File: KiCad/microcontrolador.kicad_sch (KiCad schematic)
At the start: 0 parts

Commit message: he canviat el micro
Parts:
- added C2: 10uF, symbol Device:C
- added C21, C5: 100nF, symbol Device:C
- added C6, C7, C8: 0.1uF, symbol Device:C
- added PIC32MX254F128B1: ~, projecte_llums:PIC32MX254F128B, symbol PROJECTE_LLUMS:PIC32MX254F128B
- added R1, R18: 10K, symbol Device:R
- added U7: PIC24HJ128GP502-I_SO, PIC24HJ128GP502-I_SO:SOIC127P1030X265-28N, symbol PIC24HJ128GP502-I_SO:PIC24HJ128GP502-I_SO
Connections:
- new net: C21.1, PIC32MX254F128B1.1 (MCLR), R18.2
- new net: C2.2, PIC32MX254F128B1.20 (VCAP)
- new net: C5.1, R1.1, U7.1 (~{MCLR})
- new net: C8.1, U7.20 (VCAP)
- new net 3V3: PIC32MX254F128B1.28 (AVDD), R1.2, R18.1
- new net 5V: C6.1, C7.1, PIC32MX254F128B1.13 (VDD), U7.13 (VDD), U7.28 (AVDD)
- new net CANRX: PIC32MX254F128B1.17 (CANRX), U7.15 (PGEC3/ASCL1/RP6/CN24/PMD6/RB6)
- new net CANTX: PIC32MX254F128B1.18 (CANTX), U7.11 (SOSCI/RP4/CN1/PMBE/RB4)
- new net CARRETERA: PIC32MX254F128B1.12 (RA4), U7.21 (PGED2/TDI/RP10/CN16/PMD2/RB10)
- new net DIURNA: PIC32MX254F128B1.21 (RB10), U7.23 (AN12/RP12/CN14/PMD0/RB12)
- new net ENCREUAMENT: PIC32MX254F128B1.14 (RB5), U7.22 (PGEC2/TMS/RP11/CN15/PMD1/RB11)
- new net GND: C2.1, C21.2, C5.2, C6.2, C7.2, C8.2, PIC32MX254F128B1.19 (VSS), PIC32MX254F128B1.27 (AVSS), PIC32MX254F128B1.8 (VSS), U7.19 (VSS), U7.27 (AVSS), U7.8 (VSS)
- new net I2C_SCL: PIC32MX254F128B1.5 (I2C_SCL), U7.17 (TCK/SCL1/RP8/CN22/PMD4/RB8)
- new net I2C_SDA: PIC32MX254F128B1.6 (I2C_SDA), U7.18 (TDO/SDA1/RP9/CN21/PMD3/RB9)
- new net INTERM. DRT: PIC32MX254F128B1.23 (RB12), U7.25 (AN10/RTCC/RP14/CN12/PMWR/RB14)
- new net INTERM. ESQ: PIC32MX254F128B1.22 (RB11), U7.24 (AN11/RP13/CN13/PMRD/RB13)
- new net NETEJA-FARS: PIC32MX254F128B1.24 (RB13), U7.26 (AN9/RP15/CN11/PMCS1/RB15)
- new net PMW: PIC32MX254F128B1.25 (PWM), U7.6 (AN4/C1IN-/RP2/CN6/RB2)
- new net UART_RX: PIC32MX254F128B1.16 (UART_RX), U7.16 (INT0/RP7/CN23/PMD5/RB7)
- new net UART_TX: PIC32MX254F128B1.15 (UART_TX), U7.14 (PGED3/ASDA1/RP5/CN27/PMD7/RB5)
- no-connect marks 0 -> 16
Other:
- note added: "MICROCONTROLADOR"
- note added: "Pull up a prop del pin MCLR"

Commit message: ERC i footprints
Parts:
- C5, C6, C7, C8: footprint (none) -> Capacitor_SMD:C_0805_2012Metric_Pad1.18x1.45mm_HandSolder
- R1: footprint (none) -> Resistor_SMD:R_0805_2012Metric_Pad1.20x1.40mm_HandSolder
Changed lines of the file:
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@@
+		(color 0 0 0 0)
+	)
+	(junction
+		(at 194.31 67.31)
+		(diameter 0)
 		(color 0 0 0 0)
 	)
@@
 	)
 	(symbol
+		(lib_id "power:PWR_FLAG")
+		(at 194.31 67.31 180)
+		(unit 1)
+		(exclude_from_sim no)
+		(in_bom yes)
+		(on_board yes)
+		(dnp no)
+		(property "Reference" "#FLG05"
+			(at 194.31 69.215 0)
+			(effects
+				(font
+					(size 1.27 1.27)
+				)
+				(hide yes)
+			)
+		)
+		(property "Value" "PWR_FLAG"
+			(at 194.818 71.374 0)
+			(effects
+				(font
+					(size 1.27 1.27)
+				)
+			)
+		)
+		(property "Footprint" ""
+			(at 194.31 67.31 0)
+			(effects
+				(font
+					(size 1.27 1.27)
+				)
+				(hide yes)
+			)
+		)
+		(property "Datasheet" "~"
+			(at 194.31 67.31 0)
+			(effects
+				(font
+					(size 1.27 1.27)
+				)
+				(hide yes)
+			)
+		)
+		(property "Description" "Special symbol for telling ERC where power comes from"
+			(at 194.31 67.31 0)
+			(effects
+				(font
+					(size 1.27 1.27)
+				)
+				(hide yes)
+			)
+		)
+		(pin "1"
+		)
+		(instances
+			(project ""
+				(path "/b4874c87-978f-427f-bc45-3635f8629977/65403977-6a27-47ce-ace7-4876548c1d8f"
+					(reference "#FLG05")
+					(unit 1)
+				)
+			)
+		)
+	)
+	(symbol
 		(lib_id "PROJECTE_LLUMS:PIC32MX254F128B")
 		(at -55.88 92.71 0)
@@
 			)
 		)
-		(property "Footprint" ""
+		(property "Footprint" "Resistor_SMD:R_0805_2012Metric_Pad1.20x1.40mm_HandSolder"
 			(at 80.518 64.77 90)
 			(effects
@@
 			)
 		)
-		(property "Footprint" ""
+		(property "Footprint" "Capacitor_SMD:C_0805_2012Metric_Pad1.18x1.45mm_HandSolder"
 			(at 227.0252 72.39 0)
 			(effects
@@
 			)
 		)
-		(property "Footprint" ""
+		(property "Footprint" "Capacitor_SMD:C_0805_2012Metric_Pad1.18x1.45mm_HandSolder"
 			(at 79.7052 82.55 0)
 			(effects
@@
 			)
 		)
-		(property "Footprint" ""
+		(property "Footprint" "Capacitor_SMD:C_0805_2012Metric_Pad1.18x1.45mm_HandSolder"
 			(at 237.1852 69.85 0)
 			(effects
@@
 			)
 		)
-		(property "Footprint" ""
+		(property "Footprint" "Capacitor_SMD:C_0805_2012Metric_Pad1.18x1.45mm_HandSolder"
 			(at 216.8652 74.93 0)
 			(effects

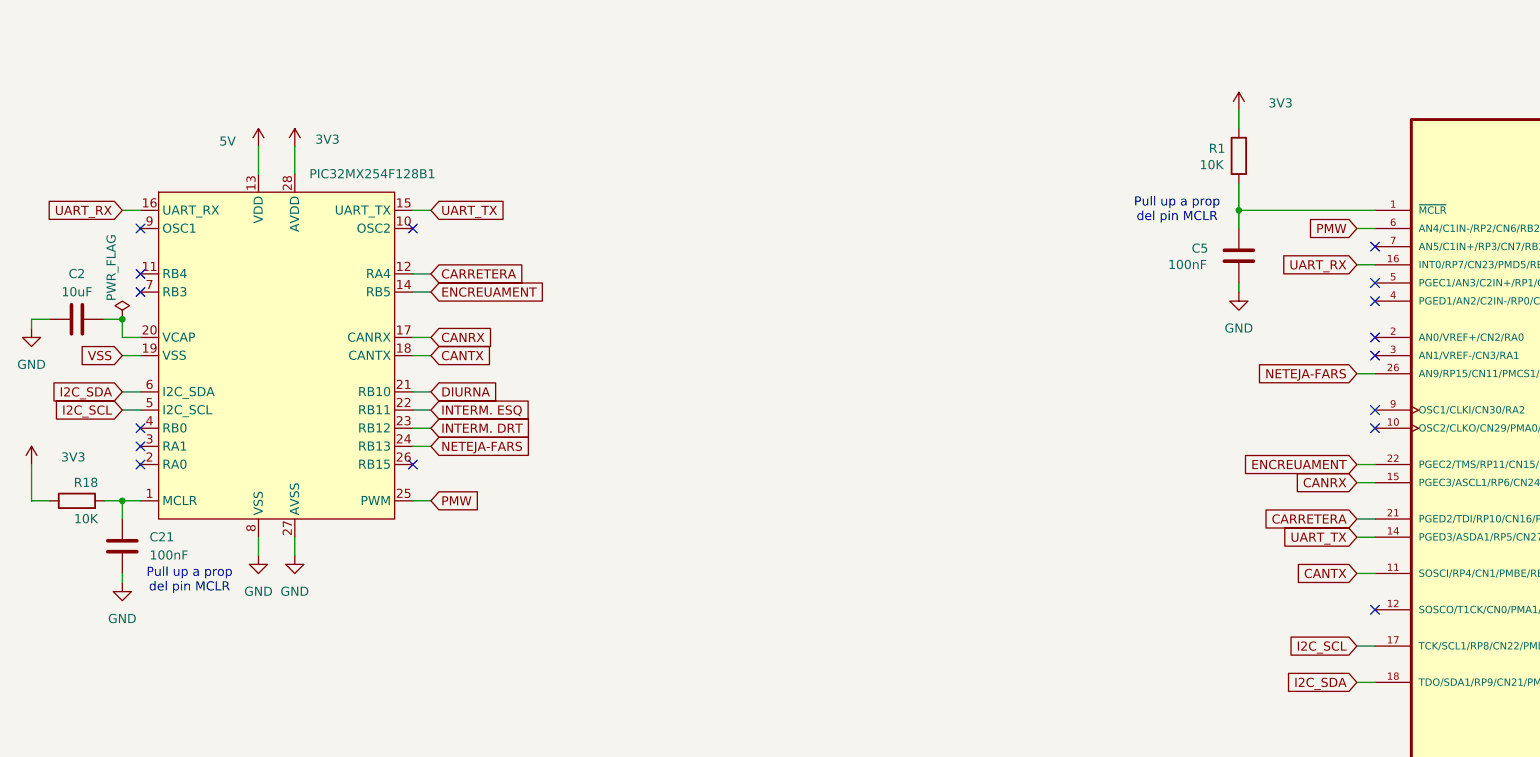
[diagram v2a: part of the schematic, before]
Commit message: placement (falten LEDs)
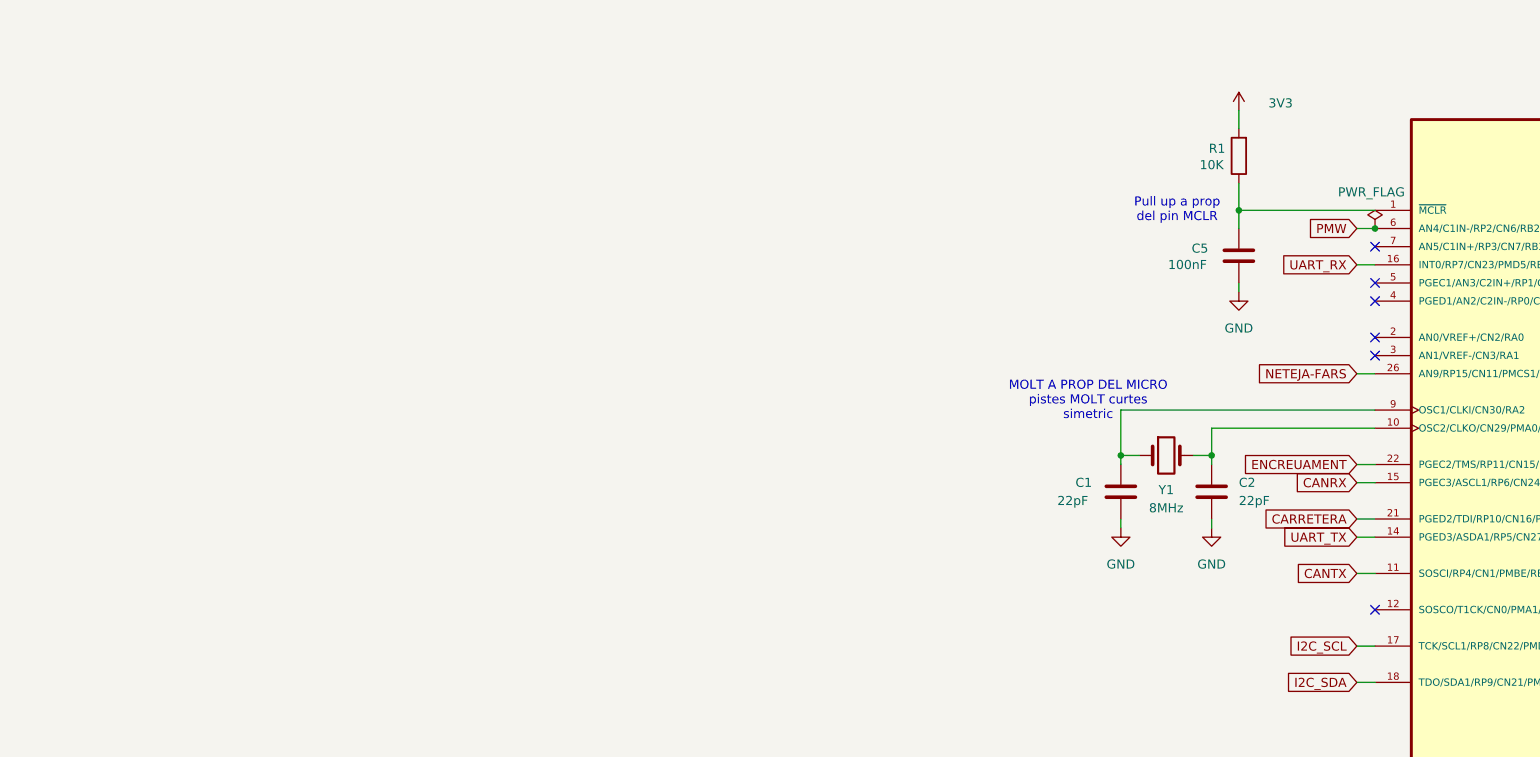
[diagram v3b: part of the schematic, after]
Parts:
- removed C21: 100nF, symbol Device:C
- removed PIC32MX254F128B1: ~, projecte_llums:PIC32MX254F128B, symbol PROJECTE_LLUMS:PIC32MX254F128B
- removed R18: 10K, symbol Device:R
- added C1: 22pF, Capacitor_SMD:C_0805_2012Metric_Pad1.18x1.45mm_HandSolder, symbol Device:C
- added Y1: 8MHz, Crystal:Crystal_SMD_3225-4Pin_3.2x2.5mm_HandSoldering, symbol Device:Crystal
- C2: value 10uF -> 22pF; footprint (none) -> Capacitor_SMD:C_0805_2012Metric_Pad1.18x1.45mm_HandSolder
- U7: footprint PIC24HJ128GP502-I_SO:SOIC127P1030X265-28N -> footprints:SOIC127P1030X265-28N
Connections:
- net GND: now also C2.2, C1.2; no longer C2.1
- net at U7.10 (OSC2/CLKO/CN29/PMA0/RA3): now also C2.1, Y1.2
- net at U7.9 (OSC1/CLKI/CN30/RA2): now also C1.1, Y1.1
- no-connect marks 16 -> 6
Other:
- note added: "MOLT A PROP DEL MICRO pistes MOLT curtes simetric"

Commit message: routing
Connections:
- net /MCLR: now reaches C5.1, R1.1, U7.1 (~{MCLR})
- net OSC2: now reaches C2.1, U7.10 (OSC2/CLKO/CN29/PMA0/RA3), Y1.2
- net VCAP: now reaches C8.1, U7.20 (VCAP)
- net OSC1: now reaches C1.1, U7.9 (OSC1/CLKI/CN30/RA2), Y1.1
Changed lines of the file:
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@@
+		)
+	)
+	(label "{slash}MCLR"
+		(at 83.82 72.39 0)
+		(effects
+			(font
+				(size 1.27 1.27)
+			)
+			(justify left bottom)
+		)
+	)
+	(label "VCAP"
+		(at 200.66 67.31 0)
+		(effects
+			(font
+				(size 1.27 1.27)
+			)
+			(justify left bottom)
+		)
+	)
+	(label "OSC1"
+		(at 81.28 100.33 0)
+		(effects
+			(font
+				(size 1.27 1.27)
+			)
+			(justify left bottom)
+		)
+	)
+	(label "OSC2"
+		(at 81.28 102.87 0)
+		(effects
+			(font
+				(size 1.27 1.27)
+			)
+			(justify left bottom)
 		)
 	)

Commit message: correcció d'errors CADLAB, falten els de llums i un parell que no entenc
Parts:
- added J3: Conn_01x03, Connector_PinHeader_2.54mm:PinHeader_1x03_P2.54mm_Vertical, symbol Connector_Generic:Conn_01x03
- added R16, R17: 100, Resistor_SMD:R_0805_2012Metric_Pad1.20x1.40mm_HandSolder, symbol Device:R
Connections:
- net GND: now also J3.3 (Pin_3)
- net UART_RX: now also R17.1
- net UART_TX: now also R16.1
- new net CON1: J3.1 (Pin_1), R16.2
- new net CON2: J3.2 (Pin_2), R17.2
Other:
- note added: "USART/DEBUG"
- moved on the sheet: C1, C2, C5, C6, C7, C8, R1, U7, Y1

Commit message: alguns errors de CADLAB i he canivat d'ordre els LEDs i els drivers a la PCB.
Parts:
- removed J3: Conn_01x03, Connector_PinHeader_2.54mm:PinHeader_1x03_P2.54mm_Vertical, symbol Connector_Generic:Conn_01x03
- removed R16, R17: 100, Resistor_SMD:R_0805_2012Metric_Pad1.20x1.40mm_HandSolder, symbol Device:R
- added J2: DE9_Pins_MountingHoles, Connector_Dsub:DSUB-9_Pins_Horizontal_P2.77x2.84mm_EdgePinOffset4.94mm_Housed_MountingHolesOffset4.94mm, symbol Connector:DE9_Pins_MountingHoles
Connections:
- net GND: now also J2.5
- net UART_RX: now also J2.2
- net UART_TX: now also J2.3
- net 3V3 renamed +3V3
- net 5V renamed +5V
- net +5V: now also J2.1
- no-connect marks 6 -> 12
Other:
- note added: "2026-04-20"
- note added: "Curs 2025/2026 Eines de Disseny Martina Camprubí, Clara Rosaura Universitat de Barcelona"
- note added: "Placa Pràctica 5"

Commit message: modificacions cadlab
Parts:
- removed U7: PIC24HJ128GP502-I_SO, footprints:SOIC127P1030X265-28N, symbol PIC24HJ128GP502-I_SO:PIC24HJ128GP502-I_SO
- added C_out3: 100nF, Capacitor_SMD:C_0805_2012Metric_Pad1.18x1.45mm_HandSolder, symbol Device:C
- added J5: DE9_Pins_MountingHoles, Connector_Dsub:DSUB-9_Pins_Horizontal_P2.77x2.84mm_EdgePinOffset4.94mm_Housed_MountingHolesOffset4.94mm, symbol Connector:DE9_Pins_MountingHoles
- added R13: 12O, Resistor_SMD:R_0805_2012Metric_Pad1.20x1.40mm_HandSolder, symbol Device:R
- added R14: 10k, Resistor_SMD:R_0805_2012Metric_Pad1.20x1.40mm_HandSolder, symbol Device:R
- added U2: ~, symbol PROJECTE_LLUMS:PIC24HJ128GP502
- added U4: MCP2551-I-SN, Package_SO:SOIC-8_3.9x4.9mm_P1.27mm, symbol Interface_CAN_LIN:MCP2551-I-SN
- added U7: PIC24HJ128GP502, projecte_llums:SOIC127P1030X265-28N, symbol PROJECTE_LLUMS:PIC24HJ128GP502
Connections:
- net +5V: now also J5.1, U7.13 (VDD), U7.28 (AVDD)
- net CANRX: now also U4.4 (RXD), U7.15 (CANRX)
- net CANTX: now also U4.1 (TXD), U7.11 (CANTX)
- net CARRETERA: now also U7.21 (RB10)
- net DIURNA: now also U7.23 (RB12)
- net ENCREUAMENT: now also U7.22 (RB11)
- net GND: now also C_out3.1, J5.5, R14.2, U4.2 (VSS), U7.19 (VSS), U7.27 (AVSS), U7.8 (VSS)
- net I2C_SCL: now also U7.17 (I2C_SCL)
- net I2C_SDA: now also U7.18 (12C_SDA)
- net INTERM. DRT: now also U7.25 (RB14)
- net INTERM. ESQ: now also U7.24 (RB13)
- net NETEJA-FARS: now also U7.26 (RB15)
- net OSC1: now also U7.9 (OSC1)
- net OSC2: now also U7.10 (OSC2)
- net UART_RX: now also U7.16 (UART_RX)
- net UART_TX: now also U7.14 (UART_TX)
- net /MCLR: now also U7.1 (MCLR)
- net VCAP: no longer names the net of C8.1
- net VCAP: now also U7.20 (VCAP)
- new net CANH: J5.7, R13.1, U4.7 (CANH)
- new net CANL: J5.2, R13.2, U4.6 (CANL)
- new net Rs: R14.1, U4.8 (Rs)
- new net VDD: C_out3.2, U4.3 (VDD)
- no-connect marks 12 -> 20
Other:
- note added: "Pull up a prop del XIP"
- note added: "TRANSCIEVER"
- moved on the sheet: C1, C2, C5, C6, C7, C8, J2, R1, Y1

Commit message: correccions Manel
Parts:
- added J3: Conn_01x05, Connector_PinHeader_2.54mm:PinHeader_1x05_P2.54mm_Vertical, symbol Connector_Generic:Conn_01x05
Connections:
- net GND: now also J3.3 (Pin_3)
- net DATA: now reaches U7.4 (RB0)
- net DATA: now also J3.4 (Pin_4)
- net CLK: now reaches U7.5 (RB1)
- net CLK: now also J3.5 (Pin_5)
- net /MCLR renamed VPP_MCLR
- net VPP_MCLR: now also J3.1 (Pin_1)
- new net 5V: J3.2 (Pin_2)
- no-connect marks 20 -> 18
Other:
- note added: "PROGRAMADOR"
- moved on the sheet: C1, C2, C5, C6, C7, C8, R1, Y1
